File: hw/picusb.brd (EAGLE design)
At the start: 45.7 x 33.3 mm, 38 parts, among them Q1 BSS138, Q2 BSS138, Q3 BSS84, Q4 BSS84, U1 PIC16F1454SOIC, U2 AP7115W, X1 MINI-USB-UX60-MB-5ST

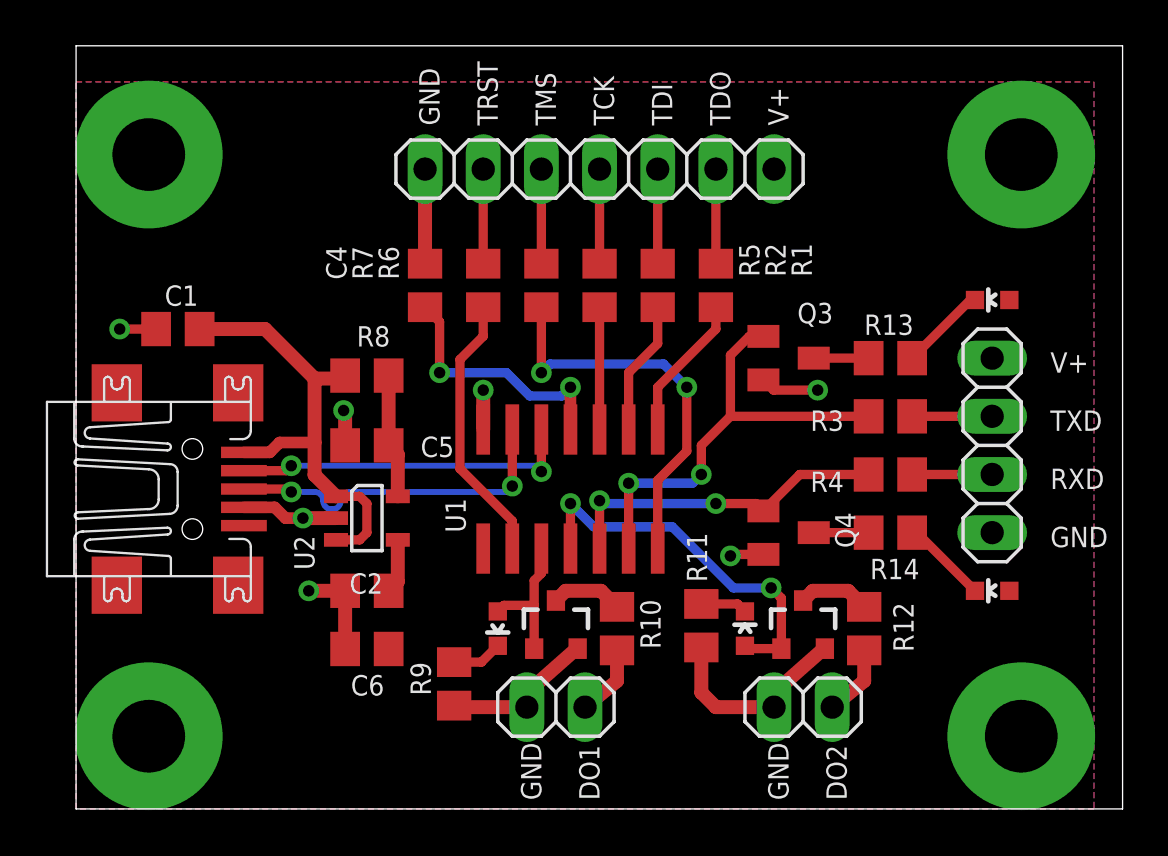
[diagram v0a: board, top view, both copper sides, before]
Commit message: moved USB connector so it is centred, added OHW logo and text
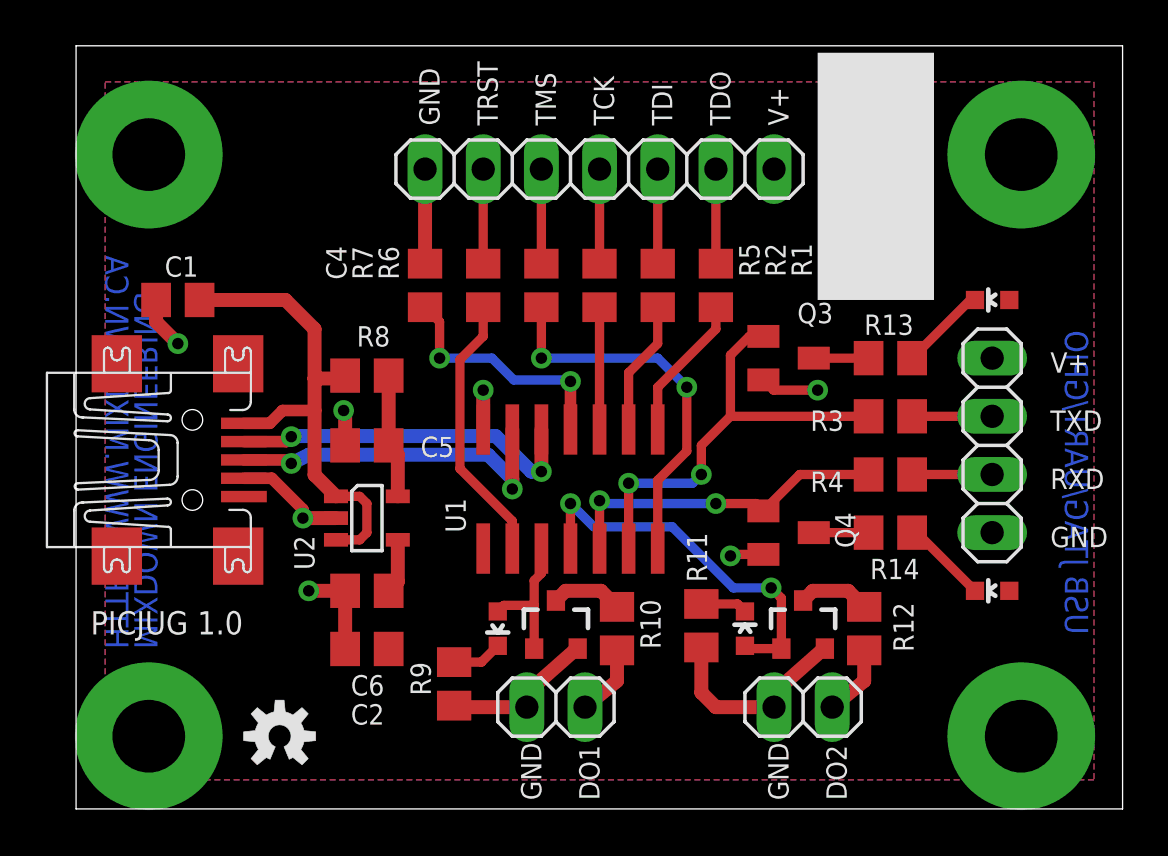
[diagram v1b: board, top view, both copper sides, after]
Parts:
- moved C1 1.27 mm to (4.45, 22.2)
- moved X1 1.27 mm to (5.08, 15.2)
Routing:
- net VUSB: track 20.3 -> 22.2 mm
- net GND: track 37.1 -> 38.6 mm
- net TMS: track 17.4 -> 16.7 mm
- net N$4: track 11.3 -> 10.7 mm
- net D_N: track 15.0 -> 15.6 mm
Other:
- board text added: "HTTP://WWW.MIXDOWN.CA"
- board text added: "MIXDOWN ENGINEERING"
- board text added: "PICJUG 1.0"
- board text added: "USB JTAG/UART/GPIO"
